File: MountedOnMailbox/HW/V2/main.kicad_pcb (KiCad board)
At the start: 2 copper layers, 24.9 x 82 mm, 34 parts, among them J1 BoxLidSensor, J2 CONSMA001-SMD-G, J3 FTDI, J4 AVR-ISP-6, Q1 IRF7341, SW1 Reset, U1 ATMEGA328P-AU-Arduino, U2 RFM95W-868S2, U3 DW01-P, U4 AP2210-3.3V, Y1 8MHz

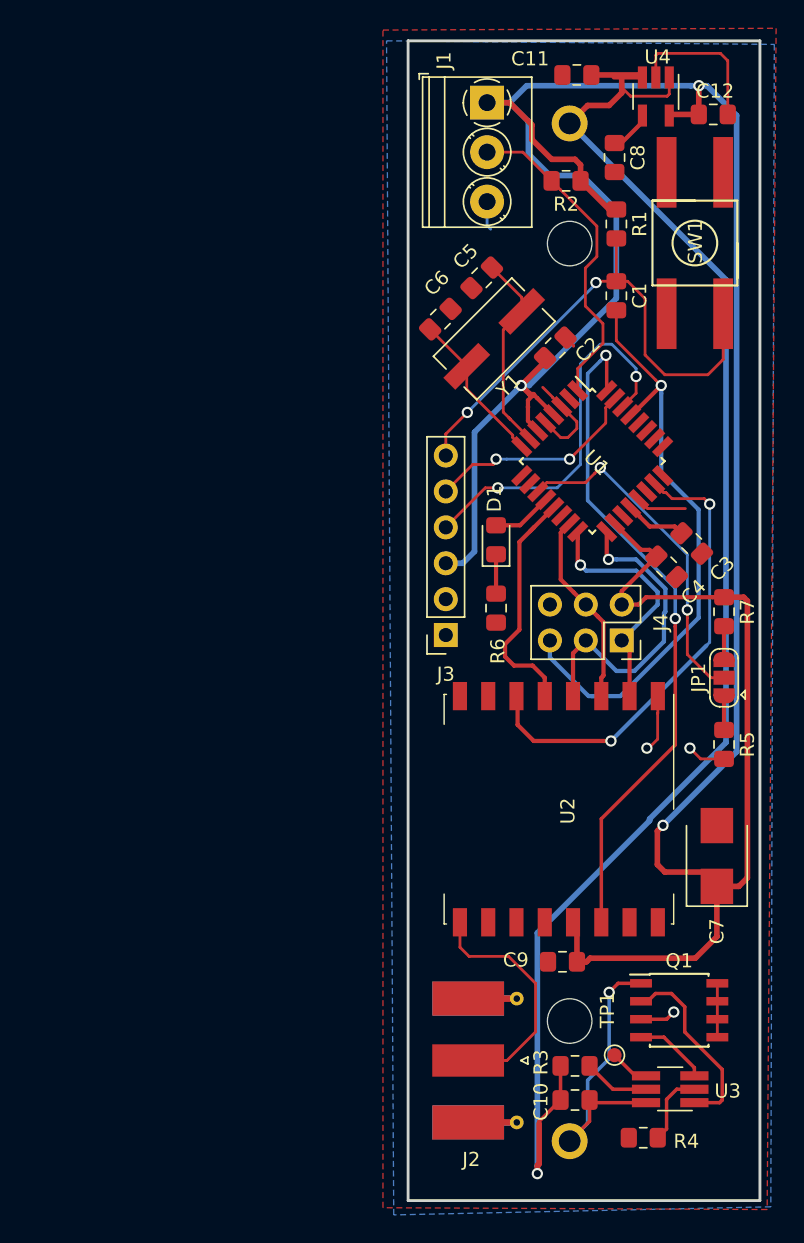
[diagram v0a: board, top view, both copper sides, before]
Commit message: Better layout
And i2c header
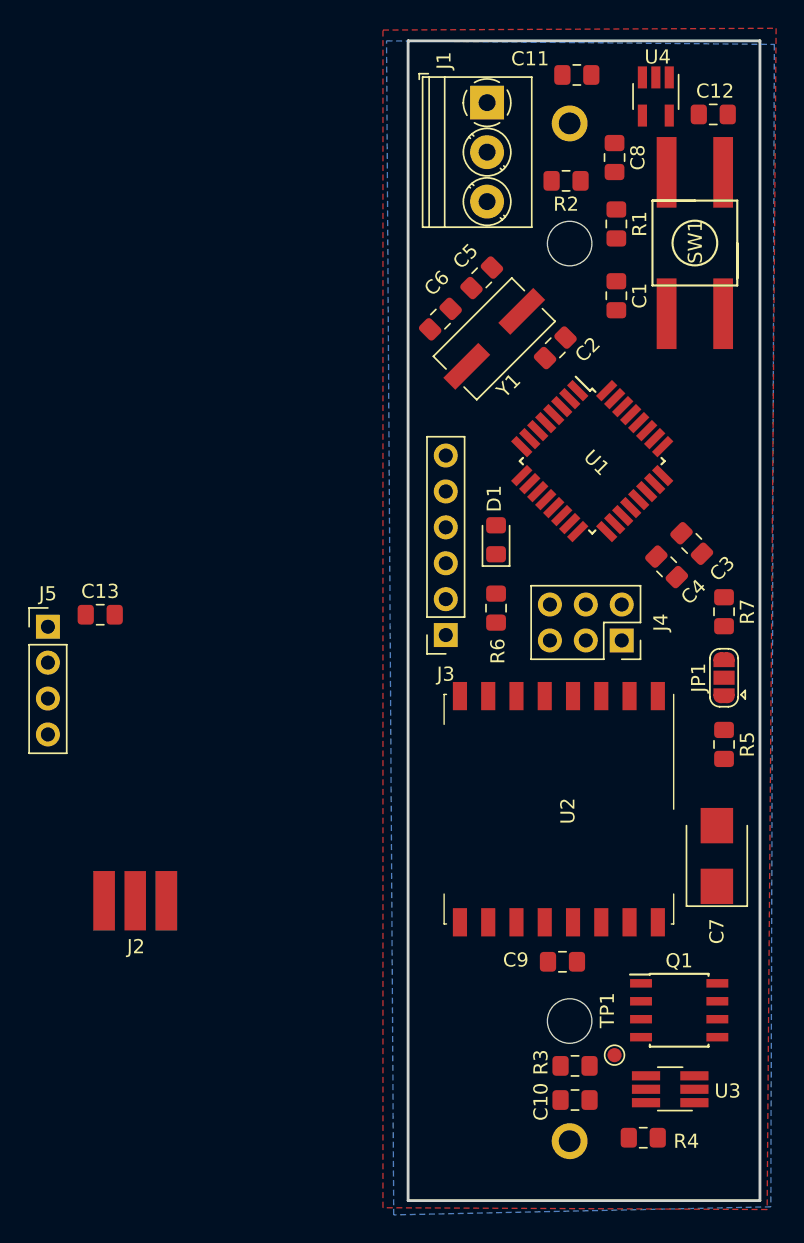
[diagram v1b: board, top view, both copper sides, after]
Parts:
- added C13: 100n, Capacitor_SMD:C_0805_2012Metric_Pad1.15x1.40mm_HandSolder, F.Cu at (107.8, 95.7)
- added J5: Conn_01x04_Female, Connector_PinHeader_2.54mm:PinHeader_1x04_P2.54mm_Vertical, F.Cu at (104.1, 96.6)
- C1: value C -> 100n
- J2: footprint Connector_Coaxial:SMA_Molex_73251-1153_EdgeMount_Horizontal -> Libs:SMA_edge connector
- moved J2 30.9 mm to (108.0, 113.2)
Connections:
- C1 pad 2: reset_in -> Net-(C1-Pad2)
- U1 pad 27: sda -> SDA
- U1 pad 28: scl -> SCL
- U1 pad 29: reset_in -> Net-(C1-Pad2)
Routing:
- net +3V3: track 205.8 -> 0.00 mm, vias 3 -> 0
- net +BATT: track 111.8 -> 0.00 mm, vias 1 -> 0
- net LoRa_INT: track 47.9 -> 0.00 mm, vias 2 -> 0
- net reset_in: track 42.8 -> 0.00 mm, vias 1 -> 0
- net GND: track 39.4 -> 0.00 mm, vias 3 -> 0
- net RST: track 37.5 -> 0.00 mm, vias 2 -> 0
- net LoRaReset: track 33.4 -> 0.00 mm, vias 2 -> 0
- net RXI: track 26.8 -> 0.00 mm, vias 2 -> 0
- net Jumper_selsction: track 24.2 -> 0.00 mm, vias 2 -> 0
- net Net-(J1-Pad2): track 23.2 -> 0.00 mm
- net SCK: track 22.3 -> 0.00 mm, vias 1 -> 0
- net Net-(B1-Pad2): track 21.8 -> 0.00 mm, vias 1 -> 0
- net MISO: track 18.0 -> 0.00 mm, vias 1 -> 0
- net Net-(J2-Pad1): track 17.2 -> 0.00 mm
- net LoRaSS: track 17.1 -> 0.00 mm
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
